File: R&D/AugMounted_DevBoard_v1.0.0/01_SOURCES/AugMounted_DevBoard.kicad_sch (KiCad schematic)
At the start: 3 parts

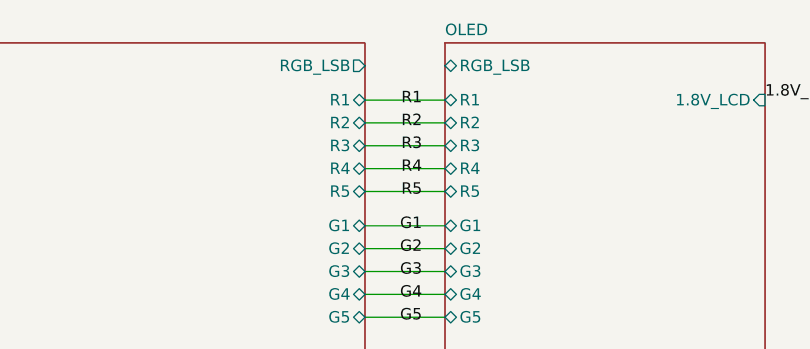
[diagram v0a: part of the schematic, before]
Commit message: Changed layout + all passive to 0402
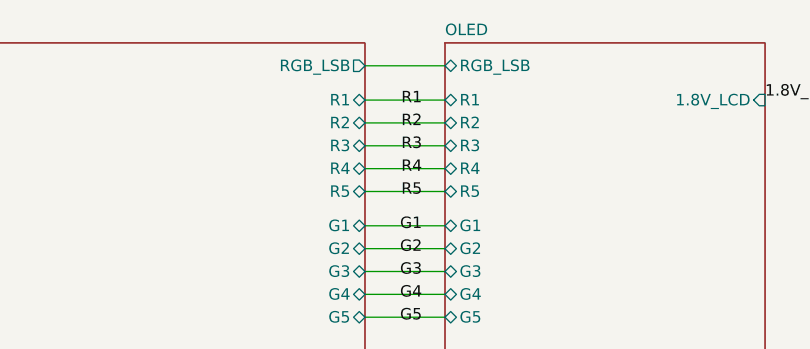
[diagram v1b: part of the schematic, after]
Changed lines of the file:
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@@
+    (stroke (width 0) (type default))
+  )
+  (wire (pts (xy 214.63 16.51) (xy 223.52 16.51))
     (stroke (width 0) (type default))
   )

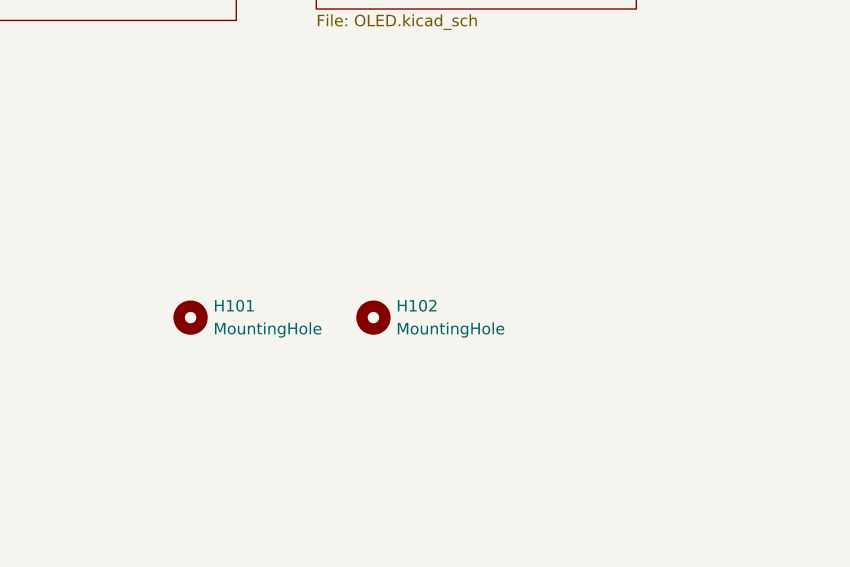
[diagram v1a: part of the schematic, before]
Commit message: Component layout is done, routing video signals is done too.
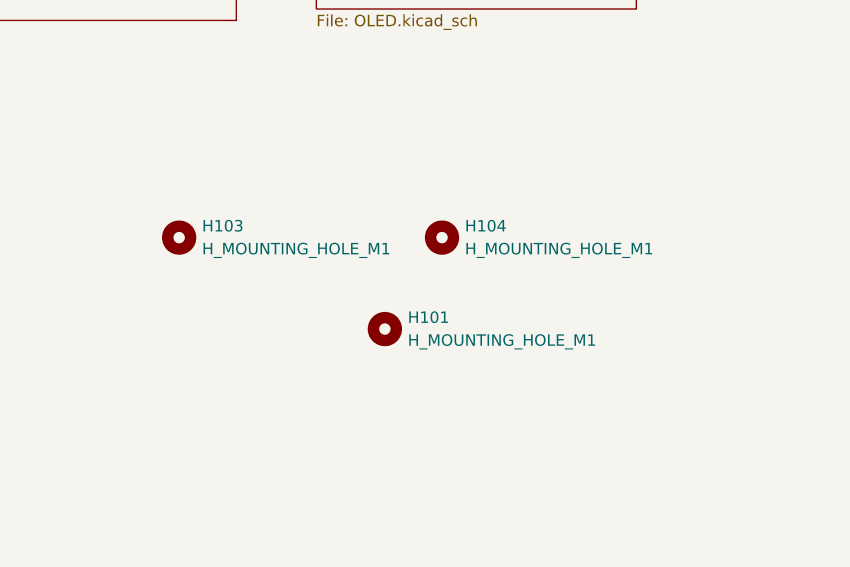
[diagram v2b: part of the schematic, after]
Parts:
- removed H101, H102: MountingHole, MountingHole:MountingHole_2.2mm_M2, symbol Mechanical:MountingHole
- added H101, H103, H104: H_MOUNTING_HOLE_M1, .mounted-lib:MountingHole_1.2mm_M1, symbol .mounted-lib:H_MOUNTING_HOLE_M1
